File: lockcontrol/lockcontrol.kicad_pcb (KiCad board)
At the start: 2 copper layers, 70.9 x 31.8 mm, 10 parts, among them J1 ButtonHeader, K1 G5Q-1A, U1 WeMos_D1_mini, U3 ULN2003, U4 Barrel_Jack_Switch, U5 Barrel_Jack_Switch

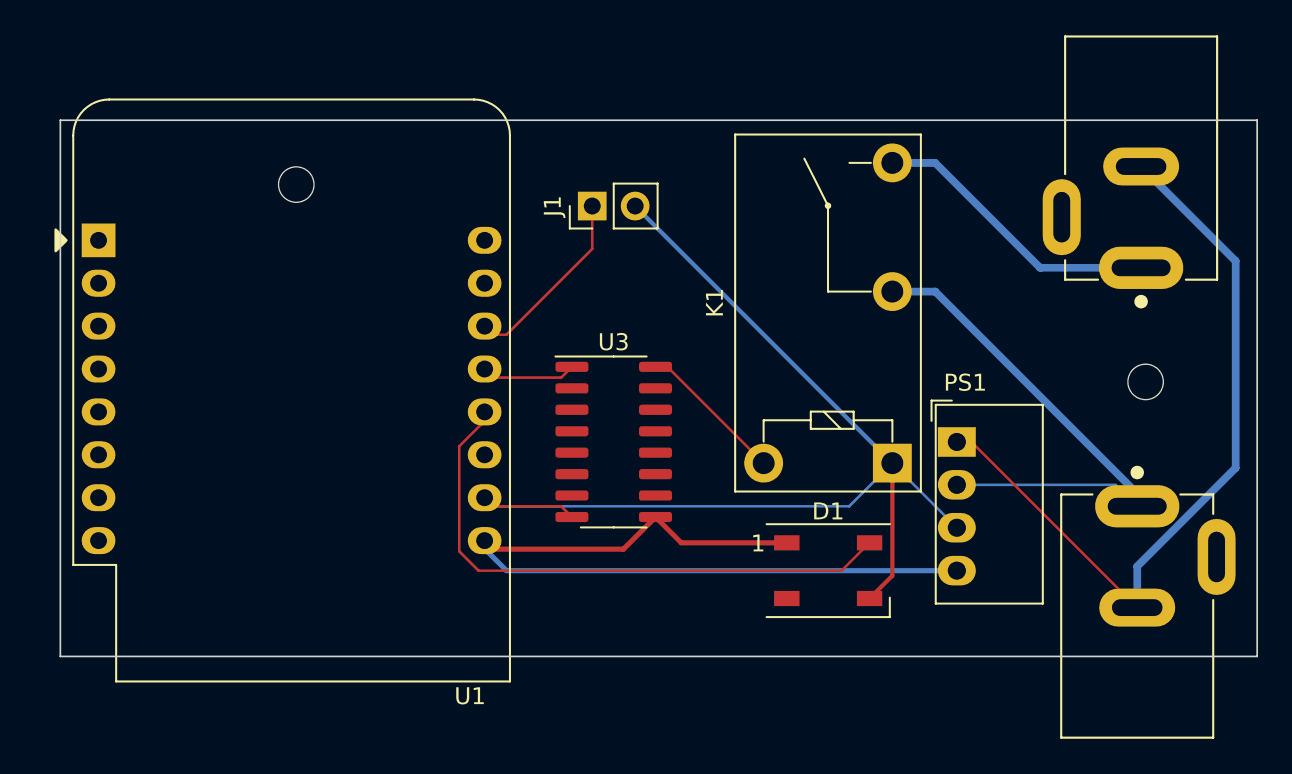
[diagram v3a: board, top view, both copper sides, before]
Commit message: relay driver is grounding, pass 5V through relay then
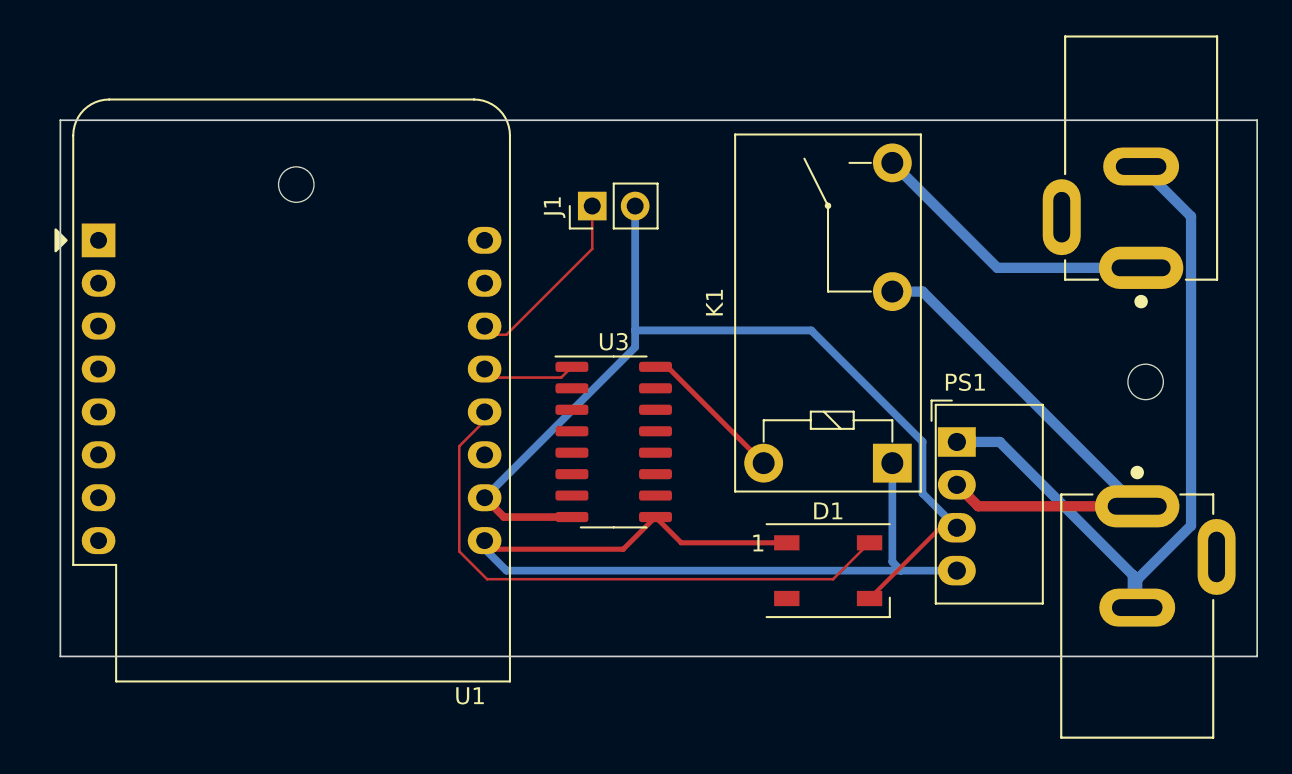
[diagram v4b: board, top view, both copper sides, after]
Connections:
- K1 pad 1: GND -> 5V
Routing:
- net GND: track 66.1 -> 59.2 mm
- net 5V: track 47.8 -> 54.3 mm
- net 12VGND: track 45.6 -> 44.4 mm
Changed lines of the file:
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@@
     (fp_line (start -1.18 -8.81) (end 18.96 -8.81) (layer "F.Fab") (width 0.1))
     (pad "1" thru_hole rect (at 0 0 270) (size 2.3 2.3) (drill 1.3) (layers *.Cu *.Mask)
-      (net 6 "GND") (pintype "passive"))
+      (net 4 "5V") (pintype "passive"))
     (pad "2" thru_hole circle (at 10.16 0 270) (size 2.3 2.3) (drill 1.3) (layers *.Cu *.Mask)
       (net 33 "12VIN") (pintype "passive"))
@@
   (segment (start 138.62 87.25) (end 144.87 87.25) (width 0.3048) (layer "F.Cu") (net 4))
   (segment (start 135.19 87.63) (end 137.095 85.725) (width 0.3048) (layer "F.Cu") (net 4))
-  (segment (start 128.27 88.9) (end 127 87.63) (width 0.3048) (layer "B.Cu") (net 4))
-  (segment (start 154.94 88.9) (end 128.27 88.9) (width 0.3048) (layer "B.Cu") (net 4))
-  (segment (start 151.12 89.2) (end 149.77 90.55) (width 0.25) (layer "F.Cu") (net 6))
-  (segment (start 151.12 82.535) (end 151.12 89.2) (width 0.25) (layer "F.Cu") (net 6))
-  (segment (start 131.51 85.09) (end 132.145 85.725) (width 0.1524) (layer "F.Cu") (net 6))
-  (segment (start 127 85.09) (end 131.51 85.09) (width 0.1524) (layer "F.Cu") (net 6))
-  (segment (start 135.89 67.31) (end 151.115 82.535) (width 0.25) (layer "B.Cu") (net 6))
-  (segment (start 148.565 85.09) (end 127 85.09) (width 0.1524) (layer "B.Cu") (net 6))
-  (segment (start 154.94 86.36) (end 151.12 82.54) (width 0.1524) (layer "B.Cu") (net 6))
-  (segment (start 151.115 82.535) (end 151.12 82.535) (width 0.25) (layer "B.Cu") (net 6))
-  (segment (start 151.12 82.54) (end 151.12 82.535) (width 0.1524) (layer "B.Cu") (net 6))
-  (segment (start 151.12 82.535) (end 148.565 85.09) (width 0.1524) (layer "B.Cu") (net 6))
-  (segment (start 125.476 87.76066) (end 126.61534 88.9) (width 0.1524) (layer "F.Cu") (net 8))
+  (segment (start 128.27 88.9) (end 127 87.63) (width 0.4572) (layer "B.Cu") (net 4))
+  (segment (start 151.12 88.382) (end 151.12 82.535) (width 0.4572) (layer "B.Cu") (net 4))
+  (segment (start 151.638 88.9) (end 128.27 88.9) (width 0.4572) (layer "B.Cu") (net 4))
+  (segment (start 154.94 88.9) (end 151.638 88.9) (width 0.4572) (layer "B.Cu") (net 4))
+  (segment (start 151.638 88.9) (end 151.12 88.382) (width 0.4572) (layer "B.Cu") (net 4))
+  (segment (start 153.96 86.36) (end 149.77 90.55) (width 0.25) (layer "F.Cu") (net 6))
+  (segment (start 128.12 85.725) (end 132.145 85.725) (width 0.4572) (layer "F.Cu") (net 6))
+  (segment (start 154.94 86.36) (end 153.96 86.36) (width 0.25) (layer "F.Cu") (net 6))
+  (segment (start 126.977 84.582) (end 128.12 85.725) (width 0.4572) (layer "F.Cu") (net 6))
+  (segment (start 135.89 67.31) (end 135.89 74.676) (width 0.4572) (layer "B.Cu") (net 6))
+  (segment (start 135.89 74.676) (end 135.89 75.669) (width 0.4572) (layer "B.Cu") (net 6))
+  (segment (start 135.89 75.669) (end 126.977 84.582) (width 0.4572) (layer "B.Cu") (net 6))
+  (segment (start 152.908 84.328) (end 154.94 86.36) (width 0.4572) (layer "B.Cu") (net 6))
+  (segment (start 152.908 81.261) (end 152.908 84.328) (width 0.4572) (layer "B.Cu") (net 6))
+  (segment (start 135.89 74.676) (end 146.323 74.676) (width 0.4572) (layer "B.Cu") (net 6))
+  (segment (start 146.323 74.676) (end 152.908 81.261) (width 0.4572) (layer "B.Cu") (net 6))
+  (segment (start 127 80.01) (end 125.476 81.534) (width 0.1524) (layer "F.Cu") (net 8))
   (segment (start 125.476 81.534) (end 125.476 87.76066) (width 0.1524) (layer "F.Cu") (net 8))
-  (segment (start 127 80.01) (end 125.476 81.534) (width 0.1524) (layer "F.Cu") (net 8))
-  (segment (start 148.12 88.9) (end 149.77 87.25) (width 0.1524) (layer "F.Cu") (net 8))
-  (segment (start 126.61534 88.9) (end 148.12 88.9) (width 0.1524) (layer "F.Cu") (net 8))
+  (segment (start 147.612 89.408) (end 149.77 87.25) (width 0.1524) (layer "F.Cu") (net 8))
+  (segment (start 125.476 87.76066) (end 127.12334 89.408) (width 0.1524) (layer "F.Cu") (net 8))
+  (segment (start 127.12334 89.408) (end 147.612 89.408) (width 0.1524) (layer "F.Cu") (net 8))
   (segment (start 128.27 74.93) (end 133.35 69.85) (width 0.1524) (layer "F.Cu") (net 9))
   (segment (start 133.35 69.85) (end 133.35 67.31) (width 0.1524) (layer "F.Cu") (net 9))
   (segment (start 127 74.93) (end 128.27 74.93) (width 0.1524) (layer "F.Cu") (net 9))
-  (segment (start 165.85 70.97) (end 159.875 70.97) (width 0.4572) (layer "B.Cu") (net 14))
-  (segment (start 159.875 70.97) (end 153.66 64.755) (width 0.4572) (layer "B.Cu") (net 14))
-  (segment (start 153.66 64.755) (end 151.12 64.755) (width 0.4572) (layer "B.Cu") (net 14))
-  (segment (start 137.8 76.835) (end 143.5 82.535) (width 0.1524) (layer "F.Cu") (net 15))
+  (segment (start 165.85 70.97) (end 157.335 70.97) (width 0.6096) (layer "B.Cu") (net 14))
+  (segment (start 157.335 70.97) (end 151.12 64.755) (width 0.6096) (layer "B.Cu") (net 14))
+  (segment (start 137.8 76.835) (end 143.5 82.535) (width 0.3048) (layer "F.Cu") (net 15))
   (segment (start 137.095 76.835) (end 137.8 76.835) (width 0.1524) (layer "F.Cu") (net 15))
   (segment (start 127 77.47) (end 131.51 77.47) (width 0.1524) (layer "F.Cu") (net 16))
   (segment (start 131.51 77.47) (end 132.145 76.835) (width 0.1524) (layer "F.Cu") (net 16))
-  (segment (start 153.66 72.375) (end 151.12 72.375) (width 0.4572) (layer "B.Cu") (net 33))
-  (segment (start 153.66 72.375) (end 165.62 84.335) (width 0.4572) (layer "B.Cu") (net 33))
-  (segment (start 165.62 84.335) (end 165.62 85.09) (width 0.4572) (layer "B.Cu") (net 33))
-  (segment (start 154.94 83.82) (end 164.35 83.82) (width 0.1524) (layer "B.Cu") (net 33))
-  (segment (start 164.35 83.82) (end 165.62 85.09) (width 0.1524) (layer "B.Cu") (net 33))
-  (segment (start 154.94 81.28) (end 155.81 81.28) (width 0.1524) (layer "F.Cu") (net 34))
-  (segment (start 155.81 81.28) (end 165.62 91.09) (width 0.1524) (layer "F.Cu") (net 34))
-  (segment (start 171.45 82.816582) (end 165.62 88.646582) (width 0.4572) (layer "B.Cu") (net 34))
-  (segment (start 165.85 64.97) (end 171.45 70.57) (width 0.4572) (layer "B.Cu") (net 34))
-  (segment (start 171.45 70.57) (end 171.45 82.816582) (width 0.4572) (layer "B.Cu") (net 34))
-  (segment (start 165.62 88.646582) (end 165.62 91.09) (width 0.4572) (layer "B.Cu") (net 34))
+  (segment (start 156.21 85.09) (end 154.94 83.82) (width 0.6096) (layer "F.Cu") (net 33))
+  (segment (start 165.62 85.09) (end 156.21 85.09) (width 0.6096) (layer "F.Cu") (net 33))
+  (segment (start 152.905 72.375) (end 165.62 85.09) (width 0.6096) (layer "B.Cu") (net 33))
+  (segment (start 151.12 72.375) (end 152.905 72.375) (width 0.6096) (layer "B.Cu") (net 33))
+  (segment (start 165.62 89.427431) (end 165.62 91.09) (width 0.6096) (layer "B.Cu") (net 34))
+  (segment (start 168.8072 67.9272) (end 168.8072 86.240231) (width 0.6096) (layer "B.Cu") (net 34))
+  (segment (start 157.48 81.28) (end 154.94 81.28) (width 0.6096) (layer "B.Cu") (net 34))
+  (segment (start 168.8072 86.240231) (end 165.62 89.427431) (width 0.6096) (layer "B.Cu") (net 34))
+  (segment (start 165.354 89.154) (end 157.48 81.28) (width 0.6096) (layer "B.Cu") (net 34))
+  (segment (start 165.354 90.824) (end 165.354 89.154) (width 0.6096) (layer "B.Cu") (net 34))
+  (segment (start 165.85 64.97) (end 168.8072 67.9272) (width 0.6096) (layer "B.Cu") (net 34))
+  (segment (start 165.62 91.09) (end 165.354 90.824) (width 0.6096) (layer "B.Cu") (net 34))
 )

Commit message: capture before removing disk
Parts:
- moved J1 14.7 mm to (133.9, 82.0)
- moved U3 7.47 mm to (135.9, 88.6), turned to -90 degrees
- turned D1 to 180 degrees
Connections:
- U1 pad 12: LED -> unconnected-(U1-Pad12)
- U1 pad 7: unconnected-(U1-Pad7) -> LED
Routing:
- net SWITCH: track 5.41 -> 19.8 mm
- net LED: track 34.3 -> 45.4 mm
- net GND: track 59.2 -> 50.3 mm
- net 5V: track 54.3 -> 47.0 mm
- net BUTTON: track 11.0 -> 13.1 mm
- net Net-(K1-Pad5): track 8.77 -> 9.90 mm
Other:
- outline, holes or cut-outs redrawn
